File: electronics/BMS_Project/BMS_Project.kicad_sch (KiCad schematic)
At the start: 12 parts, among them J1 Conn_01x20_Pin, J2 Conn_01x01_Socket, J4 ESP32_power, J5 Display_power, J6 Conn_01x01_Socket, Q1 Q_PMOS_GSD, SW2 SW_SPDT, U3 Buck

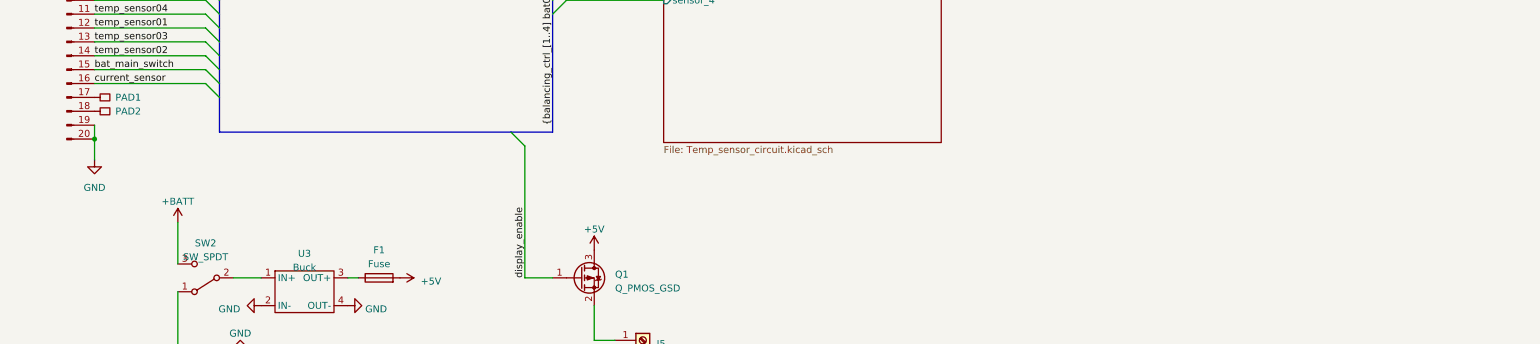
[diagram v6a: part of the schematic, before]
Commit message: Finished layout of main board and finalized lyout of cell board (added names & THI logo), changed pinout of tray plug
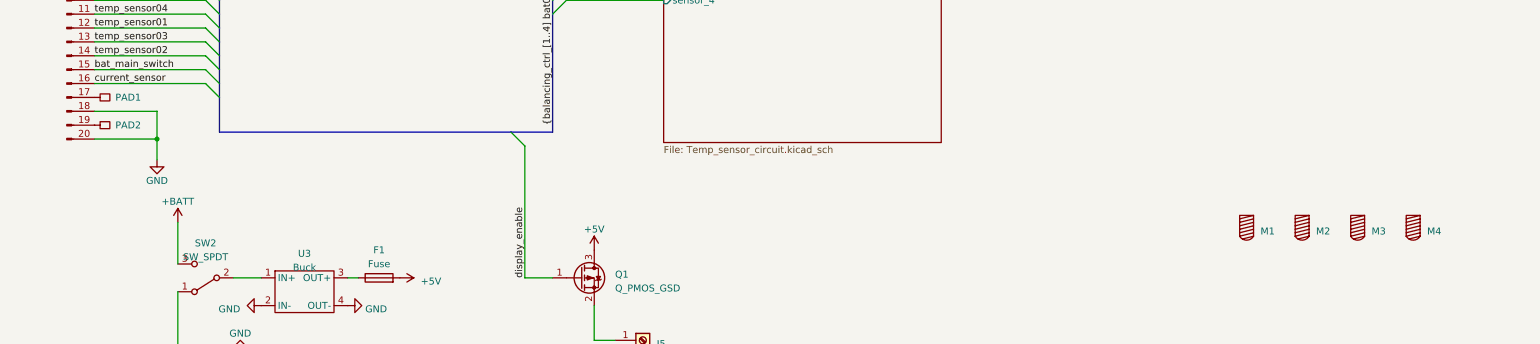
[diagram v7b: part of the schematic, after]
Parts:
- added M1, M2, M3, M4: Prototyping_Wood_Hole, BMS_lib:Prototyping_Wood_Hole, symbol BMS_lib:Prototyping_Wood_Hole
- PAD2: value Pin_18 -> Pin_19
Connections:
- net GND: now also J1.18 (Pin_18); no longer J1.19 (Pin_19)
- net at PAD2.1: now also J1.19 (Pin_19); no longer J1.18 (Pin_18)
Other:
- moved on the sheet: PAD2
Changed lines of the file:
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@@
     (comment 2 "Edited: ")
   )
-  (junction (at 30.48 140.97) (diameter 0) (color 0 0 0 0)
+  (junction (at 41.91 140.97) (diameter 0) (color 0 0 0 0)
   )
   (bus_entry (at 106.68 139.7) (size 2.54 2.54)
@@
     (stroke (width 0) (type default))
   )
+  (wire (pts (xy 30.48 140.97) (xy 41.91 140.97))
+    (stroke (width 0) (type default))
+  )
   (bus (pts (xy 53.34 102.87) (xy 53.34 100.33))
     (stroke (width 0) (type default))
@@
     (stroke (width 0) (type default))
   )
+  (wire (pts (xy 30.48 135.89) (xy 41.91 135.89))
+    (stroke (width 0) (type default))
+  )
   (bus (pts (xy 201.93 38.1) (xy 201.93 40.64))
     (stroke (width 0) (type default))
@@
     (stroke (width 0) (type default))
   )
-  (wire (pts (xy 30.48 144.78) (xy 30.48 140.97))
-    (stroke (width 0) (type default))
-  )
   (wire (pts (xy 30.48 107.95) (xy 50.8 107.95))
     (stroke (width 0) (type default))
@@
     (stroke (width 0) (type default))
   )
+  (wire (pts (xy 41.91 135.89) (xy 41.91 140.97))
+    (stroke (width 0) (type default))
+  )
   (bus (pts (xy 53.34 102.87) (xy 53.34 105.41))
     (stroke (width 0) (type default))
@@
     (stroke (width 0) (type default))
   )
+  (wire (pts (xy 41.91 140.97) (xy 41.91 144.78))
+    (stroke (width 0) (type default))
+  )
   (wire (pts (xy 181.61 69.85) (xy 181.61 99.06))
     (stroke (width 0) (type default))
@@
   )
   (wire (pts (xy 30.48 105.41) (xy 50.8 105.41))
-    (stroke (width 0) (type default))
-  )
-  (wire (pts (xy 30.48 138.43) (xy 30.48 140.97))
     (stroke (width 0) (type default))
   )
@@
     )
   )
-  (symbol (lib_id "BMS_lib:Prototyping_Pad_Data") (at 30.48 135.89 0) (unit 1)
+  (symbol (lib_id "BMS_lib:Prototyping_Pad_Data") (at 30.48 138.43 0) (unit 1)
     (in_bom yes) (on_board yes) (dnp no)
-    (property "Reference" "PAD2" (at 34.29 135.89 0)
-      (effects (font (size 1.27 1.27)) (justify left))
-    )
-    (property "Value" "Pin_18" (at 34.29 139.7 0)
+    (property "Reference" "PAD2" (at 34.29 138.43 0)
+      (effects (font (size 1.27 1.27)) (justify left))
+    )
+    (property "Value" "Pin_19" (at 34.29 142.24 0)
       (effects (font (size 1.27 1.27)) (justify left) hide)
     )
-    (property "Footprint" "BMS_lib:Prototyping_Pad_Data" (at 34.29 132.08 0)
-      (effects (font (size 1.27 1.27)) hide)
-    )
-    (property "Datasheet" "" (at 30.48 135.89 0)
+    (property "Footprint" "BMS_lib:Prototyping_Pad_Data" (at 34.29 134.62 0)
+      (effects (font (size 1.27 1.27)) hide)
+    )
+    (property "Datasheet" "" (at 30.48 138.43 0)
       (effects (font (size 1.27 1.27)) hide)
     )
@@
     )
   )
+  (symbol (lib_id "BMS_lib:Prototyping_Wood_Hole") (at 241.3 158.75 0) (unit 1)
+    (in_bom yes) (on_board yes) (dnp no) (fields_autoplaced)
+    (property "Reference" "M1" (at 243.84 157.8395 0)
+      (effects (font (size 1.27 1.27)) (justify left))
+    )
+    (property "Value" "Prototyping_Wood_Hole" (at 241.3 158.75 0)
+      (effects (font (size 1.27 1.27)) hide)
+    )
+    (property "Footprint" "BMS_lib:Prototyping_Wood_Hole" (at 241.3 158.75 0)
+      (effects (font (size 1.27 1.27)) hide)
+    )
+    (property "Datasheet" "" (at 241.3 158.75 0)
+      (effects (font (size 1.27 1.27)) hide)
+    )
+    (instances
+      (project "BMS_Project"
+        (path "/524e7f14-feb0-4ca2-9425-a347c869bfa6"
+          (reference "M1") (unit 1)
+        )
+      )
+    )
+  )
   (symbol (lib_id "Connector:Screw_Terminal_01x02") (at 130.81 177.8 0) (unit 1)
     (in_bom yes) (on_board yes) (dnp no) (fields_autoplaced)
@@
         (path "/524e7f14-feb0-4ca2-9425-a347c869bfa6"
           (reference "#PWR016") (unit 1)
+        )
+      )
+    )
+  )
+  (symbol (lib_id "BMS_lib:Prototyping_Wood_Hole") (at 271.78 158.75 0) (unit 1)
+    (in_bom yes) (on_board yes) (dnp no) (fields_autoplaced)
+    (property "Reference" "M4" (at 274.32 157.8395 0)
+      (effects (font (size 1.27 1.27)) (justify left))
+    )
+    (property "Value" "Prototyping_Wood_Hole" (at 271.78 158.75 0)
+      (effects (font (size 1.27 1.27)) hide)
+    )
+    (property "Footprint" "BMS_lib:Prototyping_Wood_Hole" (at 271.78 158.75 0)
+      (effects (font (size 1.27 1.27)) hide)
+    )
+    (property "Datasheet" "" (at 271.78 158.75 0)
+      (effects (font (size 1.27 1.27)) hide)
+    )
+    (instances
+      (project "BMS_Project"
+        (path "/524e7f14-feb0-4ca2-9425-a347c869bfa6"
+          (reference "M4") (unit 1)
         )
       )
@@
     )
   )
-  (symbol (lib_id "power:GND") (at 30.48 144.78 0) (unit 1)
-    (in_bom yes) (on_board yes) (dnp no) (fields_autoplaced)
-    (property "Reference" "#PWR012" (at 30.48 151.13 0)
-      (effects (font (size 1.27 1.27)) hide)
-    )
-    (property "Value" "GND" (at 30.48 149.86 0)
+  (symbol (lib_id "power:GND") (at 41.91 144.78 0) (unit 1)
+    (in_bom yes) (on_board yes) (dnp no)
+    (property "Reference" "#PWR012" (at 41.91 151.13 0)
+      (effects (font (size 1.27 1.27)) hide)
+    )
+    (property "Value" "GND" (at 41.91 148.59 0)
       (effects (font (size 1.27 1.27)))
     )
-    (property "Footprint" "" (at 30.48 144.78 0)
-      (effects (font (size 1.27 1.27)) hide)
-    )
-    (property "Datasheet" "" (at 30.48 144.78 0)
+    (property "Footprint" "" (at 41.91 144.78 0)
+      (effects (font (size 1.27 1.27)) hide)
+    )
+    (property "Datasheet" "" (at 41.91 144.78 0)
       (effects (font (size 1.27 1.27)) hide)
     )
@@
         )
       )
+    )
+  )
+  (symbol (lib_id "BMS_lib:Prototyping_Wood_Hole") (at 251.46 158.75 0) (unit 1)
+    (in_bom yes) (on_board yes) (dnp no) (fields_autoplaced)
+    (property "Reference" "M2" (at 254 157.8395 0)
+      (effects (font (size 1.27 1.27)) (justify left))
+    )
+    (property "Value" "Prototyping_Wood_Hole" (at 251.46 158.75 0)
+      (effects (font (size 1.27 1.27)) hide)
+    )
+    (property "Footprint" "BMS_lib:Prototyping_Wood_Hole" (at 251.46 158.75 0)
+      (effects (font (size 1.27 1.27)) hide)
+    )
+    (property "Datasheet" "" (at 251.46 158.75 0)
+      (effects (font (size 1.27 1.27)) hide)
+    )
+    (instances
+      (project "BMS_Project"
+        (path "/524e7f14-feb0-4ca2-9425-a347c869bfa6"
+          (reference "M2") (unit 1)
+        )
+      )
+    )
+  )
+  (symbol (lib_id "BMS_lib:Prototyping_Wood_Hole") (at 261.62 158.75 0) (unit 1)
+    (in_bom yes) (on_board yes) (dnp no) (fields_autoplaced)
+    (property "Reference" "M3" (at 264.16 157.8395 0)
+      (effects (font (size 1.27 1.27)) (justify left))
+    )
+    (property "Value" "Prototyping_Wood_Hole" (at 261.62 158.75 0)
+      (effects (font (size 1.27 1.27)) hide)
+    )
+    (property "Footprint" "BMS_lib:Prototyping_Wood_Hole" (at 261.62 158.75 0)
+      (effects (font (size 1.27 1.27)) hide)
+    )
+    (property "Datasheet" "" (at 261.62 158.75 0)
+      (effects (font (size 1.27 1.27)) hide)
+    )
+    (instances
+      (project "BMS_Project"
+        (path "/524e7f14-feb0-4ca2-9425-a347c869bfa6"
+          (reference "M3") (unit 1)
+        )
+      )
